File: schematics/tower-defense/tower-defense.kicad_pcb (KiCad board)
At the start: 2 copper layers, 165.1 x 76.2 mm, 6 parts, among them J1 Conn_01x28_Socket, J2 Conn_01x28_Socket, J3 Barrel_Jack_Switch, J4 Conn_01x16_Socket, J5 Conn_01x04_Socket, U1 COM-09032

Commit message: complete pcb v1
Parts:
- added C1: 0.1u, Capacitor_SMD:C_0603_1608Metric, F.Cu at (210.8, 64.2)
- added C2: 0.1u, Capacitor_SMD:C_0603_1608Metric, F.Cu at (198.6, 64.1)
- added D1: LED_ARGB, Connector_PinSocket_2.54mm:PinSocket_1x04_P2.54mm_Vertical, F.Cu at (66.8, 57.9)
- added D2: LTST-S220KGKT, Tower_Defense:status_led, F.Cu at (233.3, 44.8)
- added J4: Screw_Terminal_01x02, Tower_Defense:screw-terminal, F.Cu at (183.3, 50.2)
- added J5: hub75, Tower_Defense:hub75, F.Cu at (204.5, 50.5)
- added J8: Conn_01x03_Socket, Connector_PinSocket_2.54mm:PinSocket_1x03_P2.54mm_Vertical, F.Cu at (87.0, 51.2)
- added J9: Conn_01x04_Socket, Connector_PinSocket_2.54mm:PinSocket_1x04_P2.54mm_Vertical, F.Cu at (89.5, 69.0)
- added R1: 47, Resistor_SMD:R_0603_1608Metric, F.Cu at (71.2, 65.5)
- added R2: 47, Resistor_SMD:R_0603_1608Metric, F.Cu at (71.2, 63.0)
- added R3: 47, Resistor_SMD:R_0603_1608Metric, F.Cu at (71.2, 60.5)
- added R4: 1K, Resistor_SMD:R_0603_1608Metric, F.Cu at (229.0, 44.8)
- added SW1: SW_SPDT, Tower_Defense:power_switch, F.Cu at (228.6, 73.6)
- added U2: 74AHCT245, Tower_Defense:74HTC245, F.Cu at (215.3, 60.5)
- added U3: 74AHCT245, Tower_Defense:74HTC245, F.Cu at (203.0, 60.5)
- U1: value COM-09032 -> joystick; footprint Tower_Defense:XDCR_COM-09032 -> Tower_Defense:joystick
- moved J3 31.7 mm to (229.6, 93.6), turned to 0 degrees
- moved J2 27.8 mm to (62.6, 84.8)
- moved U1 4.50 mm to (157.9, 101.2)
- moved J7 4.44 mm to (173.4, 69.0)
- moved J6 3.82 mm to (173.4, 51.2)
- renumbered J3 to J1, J4 to J2, J5 to J3, J2 to J6, J1 to J7
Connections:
- J6 pad 1: +5V -> /V5
- J6 pad 10: /G1 -> /B1
- J6 pad 12: /R2 -> /R1
- J6 pad 13: /B2 -> /G1
- J6 pad 14: /G2 -> /R2
- J6 pad 15: /E -> /G2
- J6 pad 17: /B -> /C
- J6 pad 18: /C -> /CLK
- J6 pad 19: /D -> /OE
- J6 pad 2: +3.3V -> unconnected-(J6-Pin_2-Pad2)
- J6 pad 20: /CLK -> /LAT
- J6 pad 21: /LAT -> /D
- J6 pad 22: /OE -> /B
- J6 pad 8: /R1 -> /E
- J6 pad 9: /B1 -> /B2
- J7 pad 1: +5V -> /V5
- J7 pad 3: /LED -> /LED_R
- J7 pad 4: unconnected-(J1-Pin_4-Pad4) -> /LED_G
- J7 pad 5: unconnected-(J1-Pin_5-Pad5) -> /LED_B
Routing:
- net +3.3V: track 224.0 -> 2.72 mm, vias 0 -> 1
- net /SCL: track 1.82 -> 168.8 mm
- net /SDA: track 9.29 -> 159.1 mm
- net /B: track 0.00 -> 110.9 mm
- net /D: track 0.00 -> 107.4 mm
- net /LAT: track 0.00 -> 104.0 mm
- net /OE: track 0.00 -> 100.5 mm
- net /LED_R: track 0.00 -> 99.7 mm
- net /CLK: track 0.00 -> 97.0 mm
- net /LED_G: track 0.00 -> 96.1 mm
- net /C: track 0.00 -> 93.7 mm
- net /LED_B: track 0.00 -> 92.5 mm
- net /A: track 0.00 -> 81.6 mm
- net /G2: track 0.00 -> 78.1 mm
- net /R2: track 0.00 -> 74.6 mm
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- added copper zone on B.Cu, net +3.3V
- added copper zone on B.Cu, net /V5
- removed copper zone on B.Cu, net +5V
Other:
- board size 165.1 x 76.2 mm -> 177.8 x 76.2 mm
- board text added: "+"
- board text added: "OLED Display"
- board text added: "Purdue Proton"
- board text added: "RFID"

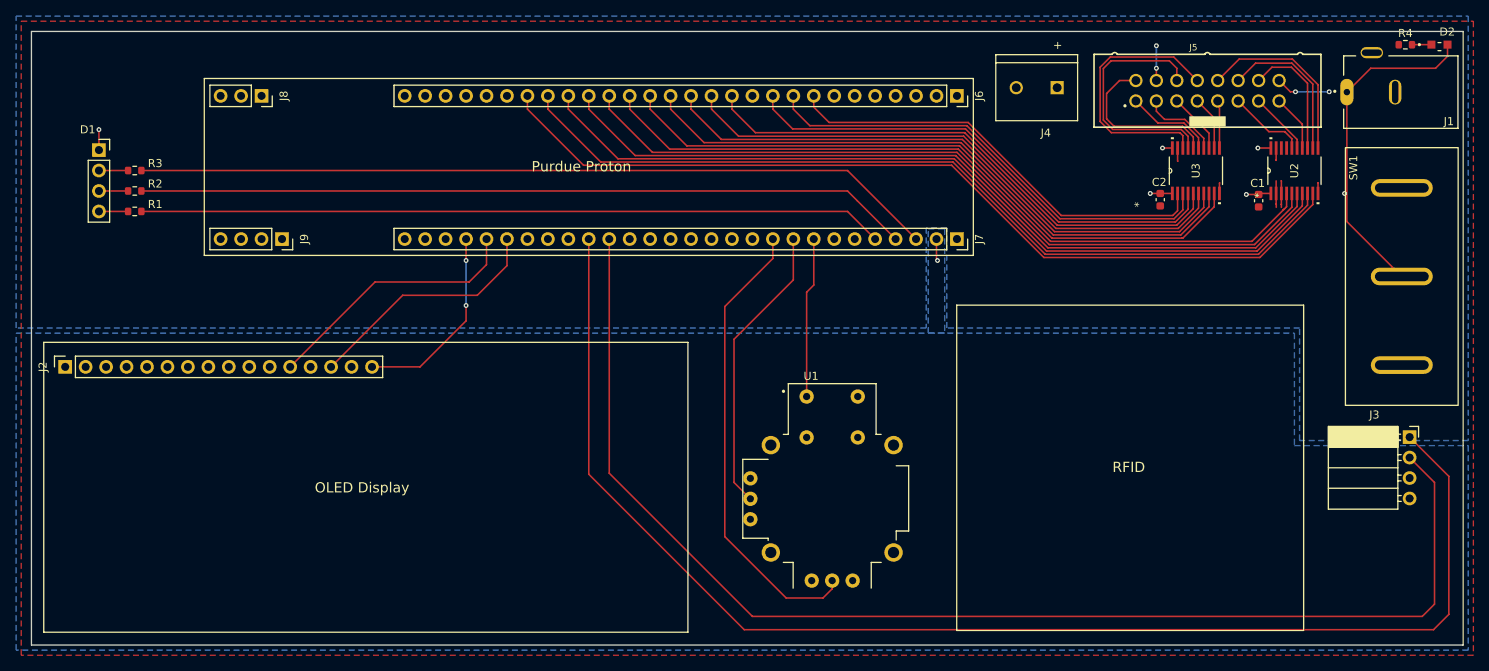
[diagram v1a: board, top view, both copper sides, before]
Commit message: pcb submission and update pins
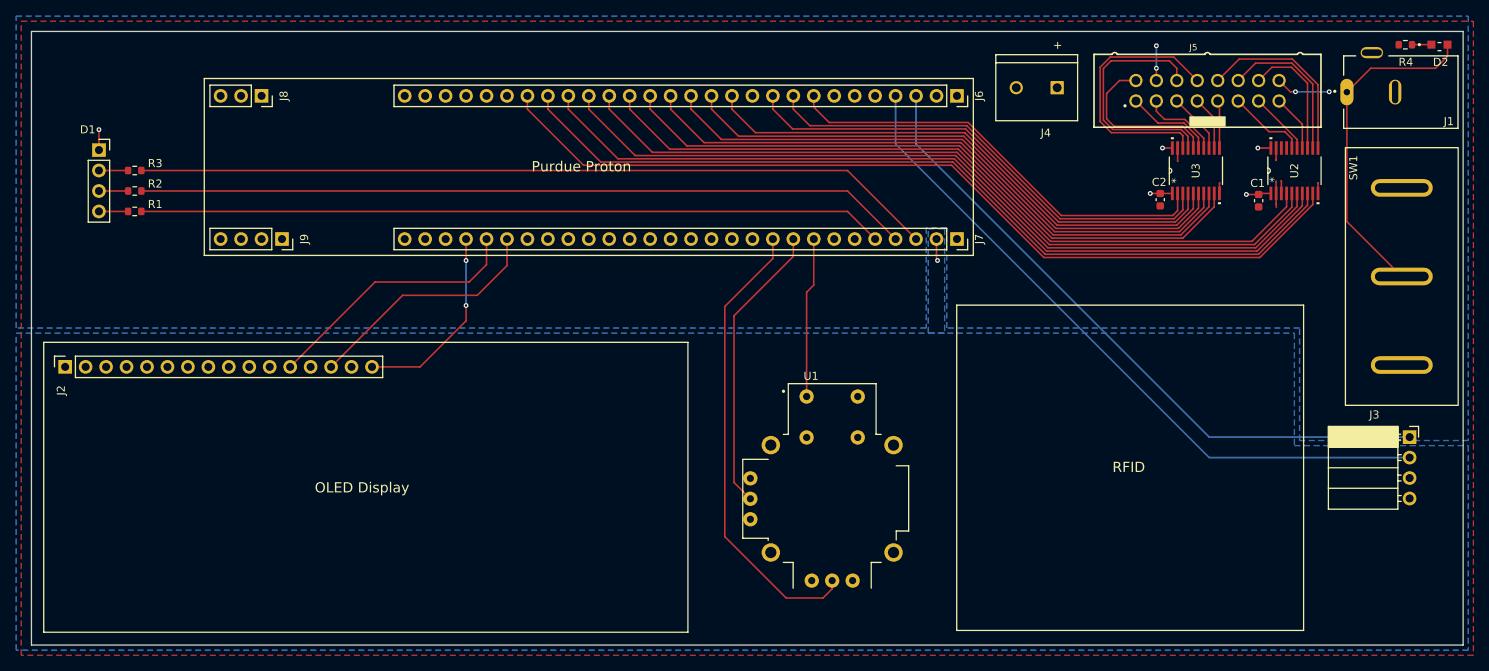
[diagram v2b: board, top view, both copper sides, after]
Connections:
- net /TX renamed /OLED_TX
- J3 pad 1: /SCL -> /RFID_TX
- J3 pad 2: /SDA -> /RFID_RX
- J6 pad 3: unconnected-(J6-Pin_3-Pad3) -> /RFID_TX
- J6 pad 4: unconnected-(J6-Pin_4-Pad4) -> /RFID_RX
- J7 pad 18: /SDA -> unconnected-(J7-Pin_18-Pad18)
- J7 pad 19: /SCL -> unconnected-(J7-Pin_19-Pad19)
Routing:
- net /SCL: track 168.8 -> 0.00 mm
- net /SDA: track 159.1 -> 0.00 mm
- net /RFID_RX: track 0.00 -> 85.9 mm
- net /RFID_TX: track 0.00 -> 82.3 mm
- net GND: track 23.6 -> 21.9 mm
- net /E: track 55.2 -> 54.5 mm
- net unconnected-(J7-Pin_18-Pad18): track 0.00 -> 0.63 mm
- net +5V: vias 1 -> 0
